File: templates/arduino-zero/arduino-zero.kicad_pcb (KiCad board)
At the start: 2 copper layers, 68.6 x 53.3 mm, 5 parts, among them U1 HOLE, U2 HOLE, U3 HOLE, U4 HOLE, U5 ARDUINO-101-SHIELD

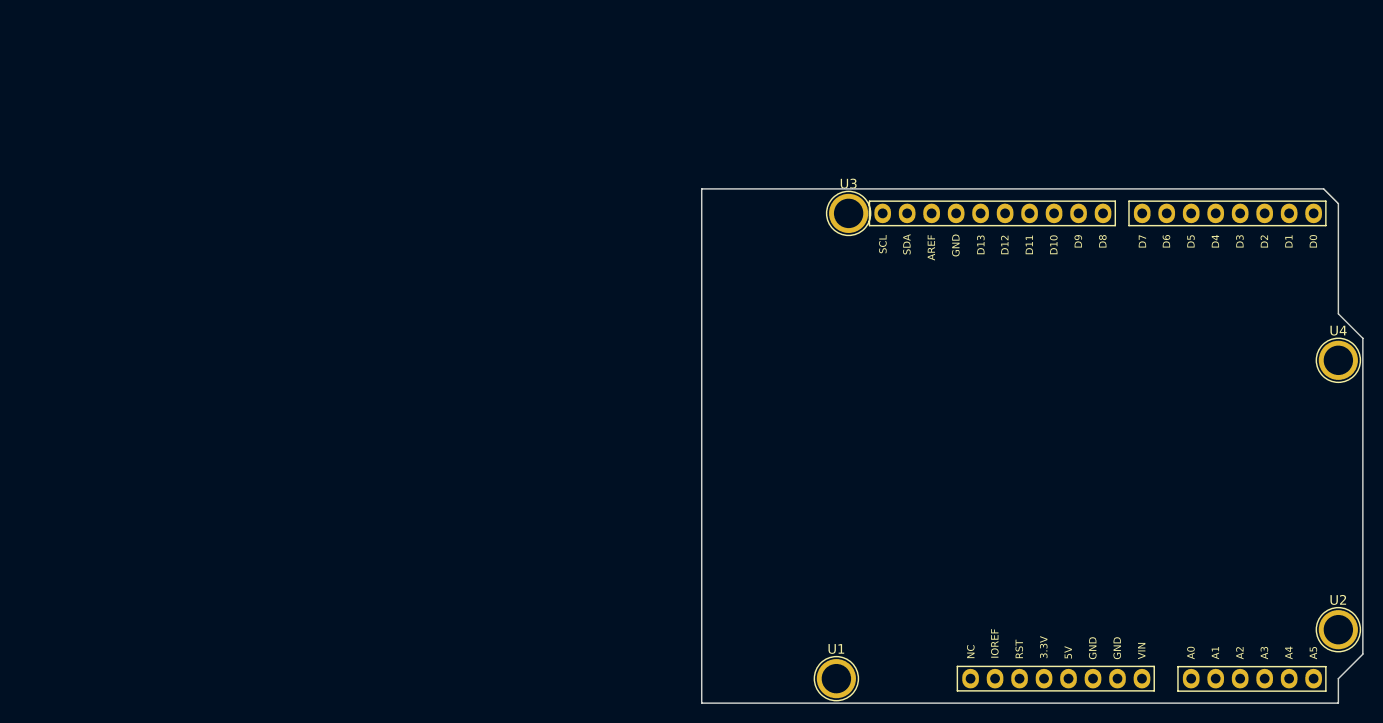
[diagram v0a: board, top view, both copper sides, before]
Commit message: Add fab notes to Dwgs.User
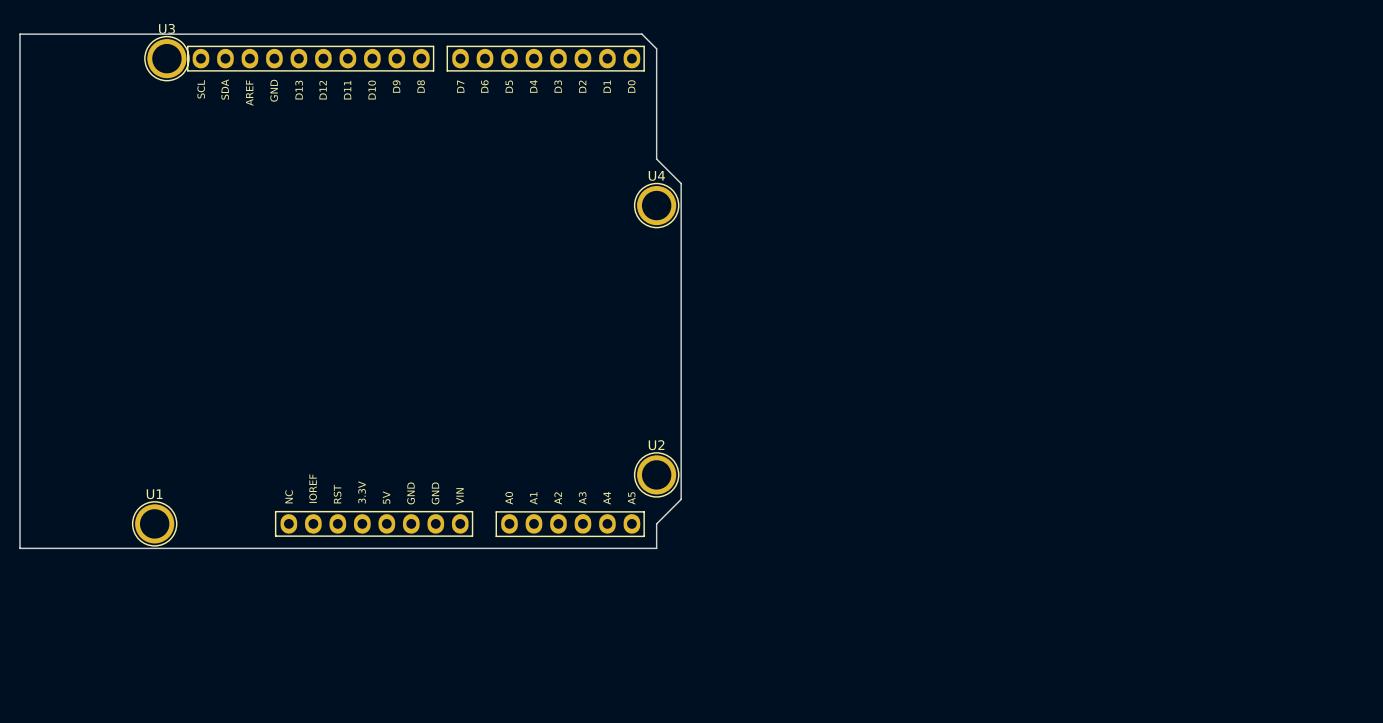
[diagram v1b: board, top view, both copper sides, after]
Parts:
- moved U1 72.5 mm to (54.3, 107.8)
- moved U2 72.5 mm to (106.3, 102.7)
- moved U4 72.5 mm to (106.3, 74.8)
- moved U3 72.5 mm to (55.5, 59.5)
- moved U5 72.5 mm to (63.1, 107.8)
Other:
- board text added: "FABRICATION NOTES 1. THIS IS A 2 LAYER BOARD. 2. EXTERNAL LAYERS SHALL HAVE 1 OZ COPPER. 3. MATERIAL: FR4 AND 0.062 INCH +/- 10% THICK. 4. BOARDS SHALL BE ROHS COMPLIANT. 5. MANUFACTURE IN ACCORDANCE WITH IPC-6012 CLASS 2 6. MASK: BOTH SIDES OF THE BOARD SHALL HAVE SOLDER MASK (ANY COLOR) OVER BARE COPPER. 7. SILK: BOTH SIDES OF THE BOARD SHALL HAVE WHITE SILKSCREEN. DO NOT PLACE SILK OVER BARE C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"
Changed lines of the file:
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@@
-(kicad_pcb (version 4) (host pcbnew 4.0.5-e0-6337~49~ubuntu16.04.1)
+(kicad_pcb (version 4) (host pcbnew 4.0.7-e2-6376~58~ubuntu16.04.1)
   (general
     (links 4)
@@
     (area 110.922999 71.488 179.653001 129.272)
     (thickness 1.6)
-    (drawings 9)
+    (drawings 10)
     (tracks 0)
     (zones 0)
@@
   )
   (module Wickerlib:ARDUINO-101-SHIELD locked (layer F.Cu)
-    (at 133.8072 123.825)
+    (at 63.0936 107.7722)
     (descr "Through hole socket strip")
     (tags "socket strip")
@@
   )
   (module ARDUINO-MOUNTING-HOLE locked (layer F.Cu)
-    (at 124.968 123.825)
+    (at 54.2544 107.7722)
     (descr "module 1 pin (ou trou mecanique de percage)")
     (tags DEV)
@@
   )
   (module ARDUINO-MOUNTING-HOLE locked (layer F.Cu)
-    (at 177.038 118.745)
+    (at 106.3244 102.6922)
     (descr "module 1 pin (ou trou mecanique de percage)")
     (tags DEV)
@@
   )
   (module ARDUINO-MOUNTING-HOLE locked (layer F.Cu)
-    (at 126.238 75.565)
+    (at 55.5244 59.5122)
     (descr "module 1 pin (ou trou mecanique de percage)")
     (tags DEV)
@@
   )
   (module ARDUINO-MOUNTING-HOLE locked (layer F.Cu)
-    (at 177.038 90.805)
+    (at 106.3244 74.7522)
     (descr "module 1 pin (ou trou mecanique de percage)")
     (tags DEV)
@@
     (pad 1 thru_hole circle (at 0 0) (size 4.064 4.064) (drill 3.048) (layers *.Cu *.Mask F.SilkS))
   )
-  (gr_line (start 177.038 74.549) (end 175.514 73.025) (angle 90) (layer Edge.Cuts) (width 0.15))
-  (gr_line (start 177.038 85.979) (end 177.038 74.549) (angle 90) (layer Edge.Cuts) (width 0.15))
-  (gr_line (start 179.578 88.519) (end 177.038 85.979) (angle 90) (layer Edge.Cuts) (width 0.15))
-  (gr_line (start 179.578 121.285) (end 179.578 88.519) (angle 90) (layer Edge.Cuts) (width 0.15))
-  (gr_line (start 177.038 123.825) (end 179.578 121.285) (angle 90) (layer Edge.Cuts) (width 0.15))
-  (gr_line (start 177.038 126.365) (end 177.038 123.825) (angle 90) (layer Edge.Cuts) (width 0.15))
-  (gr_line (start 110.998 126.365) (end 177.038 126.365) (angle 90) (layer Edge.Cuts) (width 0.15))
-  (gr_line (start 110.998 73.025) (end 110.998 126.365) (angle 90) (layer Edge.Cuts) (width 0.15))
-  (gr_line (start 175.514 73.025) (end 110.998 73.025) (angle 90) (layer Edge.Cuts) (width 0.15))
+  (gr_text "FABRICATION NOTES\n\n1. THIS IS A 2 LAYER BOARD. \n2. EXTERNAL LAYERS SHALL HAVE 1 OZ COPPER.\n3. MATERIAL: FR4 AND 0.062 INCH +/- 10% THICK.\n4. BOARDS SHALL BE ROHS COMPLIANT. \n5. MANUFACTURE IN ACCORDANCE WITH IPC-6012 CLASS 2\n6. MASK: BOTH SIDES OF THE BOARD SHALL HAVE \n   SOLDER MASK (ANY COLOR) OVER BARE COPPER. \n7. SILK: BOTH SIDES OF THE BOARD SHALL HAVE \n   WHITE SILKSCREEN. DO NOT PLACE SILK OVER BARE COPPER.\n8. FINISH: ENIG.\n9. MINIMUM TRACE WIDTH - 0.006 INCH.\n   MINIMUM SPACE - 0.006 INCH.\n   MINIMUM HOLE DIA - 0.013 INCH. \n10. MAX HOLE PLACEMENT TOLERANCE OF +/- 0.003 INCH.\n11. MAX HOLE DIAMETER TOLERANCE OF +/- 0.003 INCH AFTER PLATING." (at 120.4468 83.0072) (layer Dwgs.User)
+    (effects (font (size 2.54 2.54) (thickness 0.254)) (justify left))
+  )
+  (gr_line (start 106.3244 58.4962) (end 104.8004 56.9722) (angle 90) (layer Edge.Cuts) (width 0.15))
+  (gr_line (start 106.3244 69.9262) (end 106.3244 58.4962) (angle 90) (layer Edge.Cuts) (width 0.15))
+  (gr_line (start 108.8644 72.4662) (end 106.3244 69.9262) (angle 90) (layer Edge.Cuts) (width 0.15))
+  (gr_line (start 108.8644 105.2322) (end 108.8644 72.4662) (angle 90) (layer Edge.Cuts) (width 0.15))
+  (gr_line (start 106.3244 107.7722) (end 108.8644 105.2322) (angle 90) (layer Edge.Cuts) (width 0.15))
+  (gr_line (start 106.3244 110.3122) (end 106.3244 107.7722) (angle 90) (layer Edge.Cuts) (width 0.15))
+  (gr_line (start 40.2844 110.3122) (end 106.3244 110.3122) (angle 90) (layer Edge.Cuts) (width 0.15))
+  (gr_line (start 40.2844 56.9722) (end 40.2844 110.3122) (angle 90) (layer Edge.Cuts) (width 0.15))
+  (gr_line (start 104.8004 56.9722) (end 40.2844 56.9722) (angle 90) (layer Edge.Cuts) (width 0.15))
 )
